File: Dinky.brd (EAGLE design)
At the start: 46.4 x 16.5 mm, 15 parts, among them IC1 SAMD21

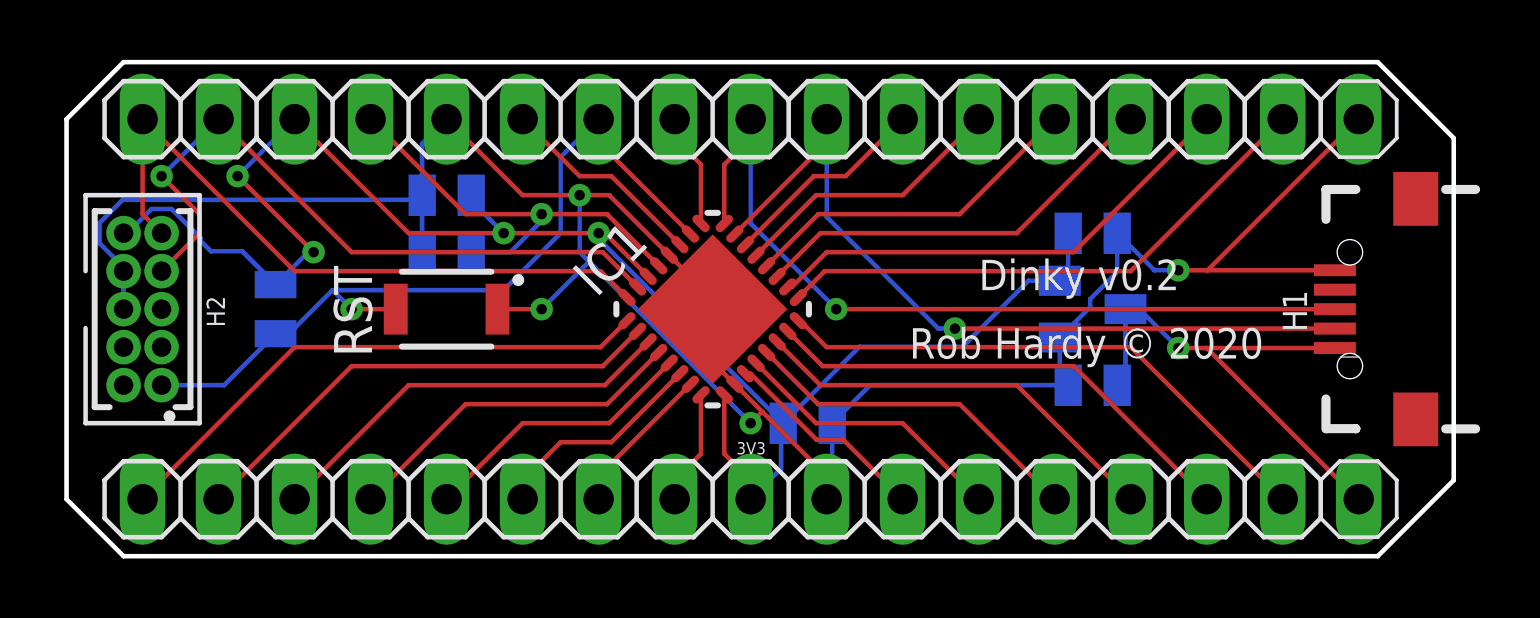
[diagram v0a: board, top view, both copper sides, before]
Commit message: Pin names
Mainly pin names and a bit of shuffling about
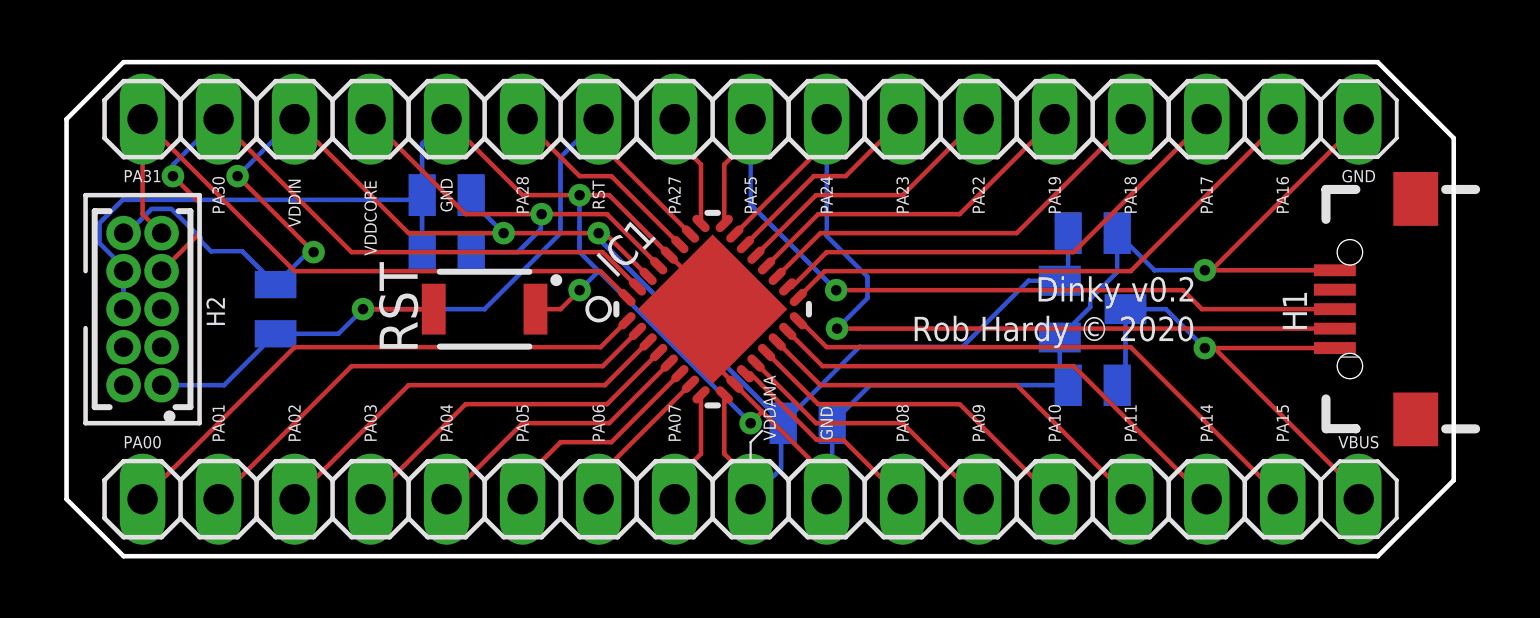
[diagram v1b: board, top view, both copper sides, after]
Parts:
- moved RST 1.27 mm to (14.0, 7.62)
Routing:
- net S$10: track 26.9 -> 29.7 mm
- net S$23: track 83.8 -> 82.8 mm
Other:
- board text added: "GND"
- board text added: "PA00"
- board text added: "PA01"
- board text added: "PA02"
- board text added: "PA03"
- board text added: "PA04"
- board text added: "PA05"
- board text added: "PA06"
- board text added: "PA07"
- board text added: "PA08"
- board text added: "PA09"
- board text added: "PA10"
- board text added: "PA11"
- board text added: "PA14"
- board text added: "PA15"
- board text added: "PA16"
- board text added: "PA17"
- board text added: "PA18"
- board text added: "PA19"
- board text added: "PA22"
- board text added: "PA23"
- board text added: "PA24"
- board text added: "PA25"
- board text added: "PA27"
- board text added: "PA28"
- board text added: "PA30"
- board text added: "PA31"
- board text added: "RST"
- board text added: "VBUS"
- board text added: "VDDANA"
- board text added: "VDDCORE"
- board text added: "VDDIN"
- board text removed: "3V3"

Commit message: Changed Button, Added LED, Added optional OSC32
Changed reset button to one more available and cheap (C&K KSR221G LFS).
Added ChipLED 0805 Red 1.8v LED to PA15 and a 100ohm resistor.
Also added pads for optional 32k osc/crystal on underside on pads PA00, PA01. Currently configured for Microcrystal CM7V-T1A and 2 12pf caps, but pads should take many combinations of crystal and caps,
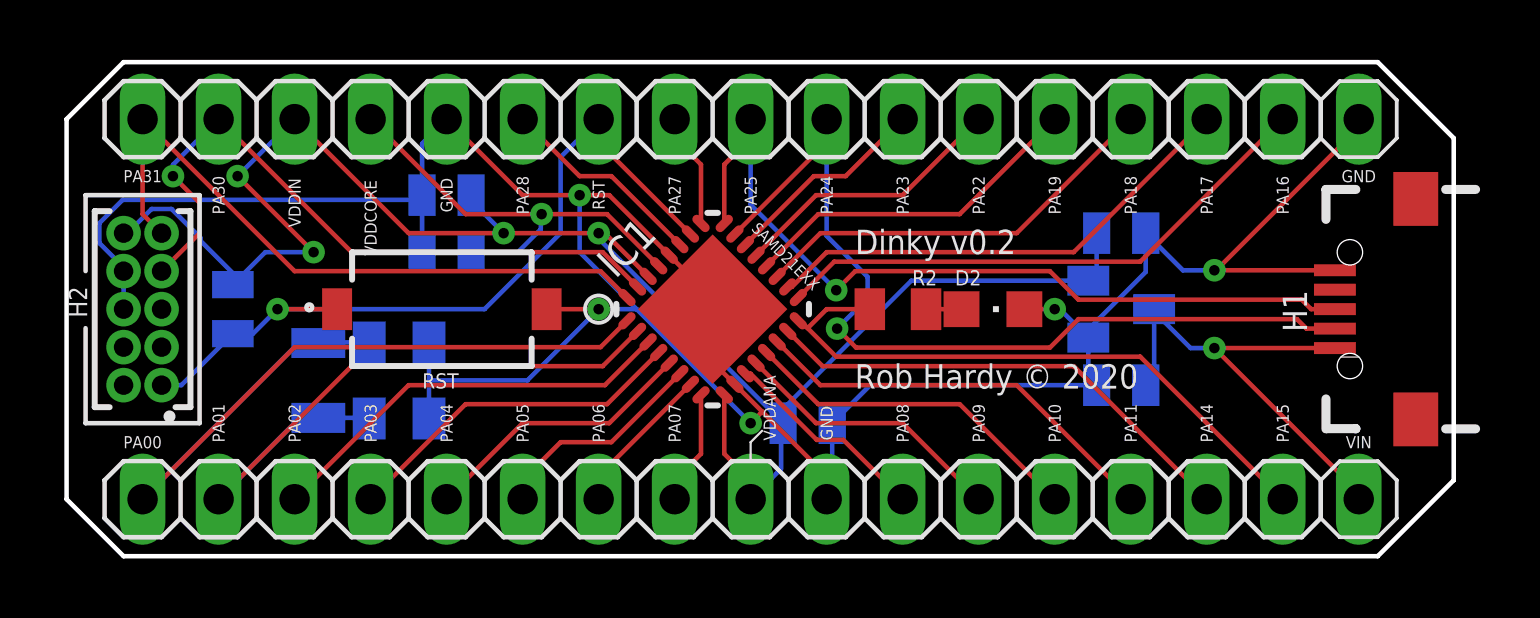
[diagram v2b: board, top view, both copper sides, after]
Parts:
- added C6, C7: (no value), adafruit:C0805K
- added D2: (no value), adafruit:CHIPLED_0805
- added R2: (no value), smd-ipc:R0805
- added Y1: (no value), CM7V-T1A-32.768kHz-12.5pF-20PP:CM7V-T1A
- RST: device B3U1000P:B3U-1000P -> KSR221G_LFS:KSR
- moved RST 1.43 mm to (12.5, 7.62)
- moved R1 1.43 mm to (5.56, 7.62)
- moved C1 0.95 mm to (35.2, 10.2)
- moved C2 0.95 mm to (35.2, 5.08)
- moved REG 0.95 mm to (35.2, 7.62)
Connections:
- removed net S$31: E$2.2, IC1.2
- removed net S$32: E$2.1, IC1.1
- new net S$24: C6.2, E$2.1, IC1.1, Y1.2
- new net S$34: C7.2, E$2.2, IC1.2, Y1.1
- new net S$5: D2.A, R2.2
- net S$17: now also R2.1
- net S$23: now also C6.1, C7.1, D2.C, RST.2; no longer RST.1
- net S$7: now also RST.1; no longer RST.2
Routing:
- net S$24: track 0.00 -> 28.4 mm
- net S$34: track 0.00 -> 22.5 mm
- net S$32: track 18.7 -> 0.00 mm
- net S$31: track 16.3 -> 0.00 mm
- net S$23: track 82.8 -> 94.7 mm, vias 4 -> 5
- net S$17: track 18.7 -> 21.0 mm
- net S$3: track 58.9 -> 60.4 mm
- net S$33: track 17.6 -> 16.3 mm
- net S$5: track 0.00 -> 1.18 mm
- net S$10: track 29.7 -> 30.5 mm
- net S$9: track 27.7 -> 28.2 mm
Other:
- board text added: "SAMD21EXX"
- board text added: "VIN"
- board text removed: "VBUS"

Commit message: Pin numbering. Larger silk text.
Changed pin numbering to minimal. Enlarged font for silkscreen printing. Moved small component names under placement as unrequired outside of placement and saves space for larger pin names and other text.
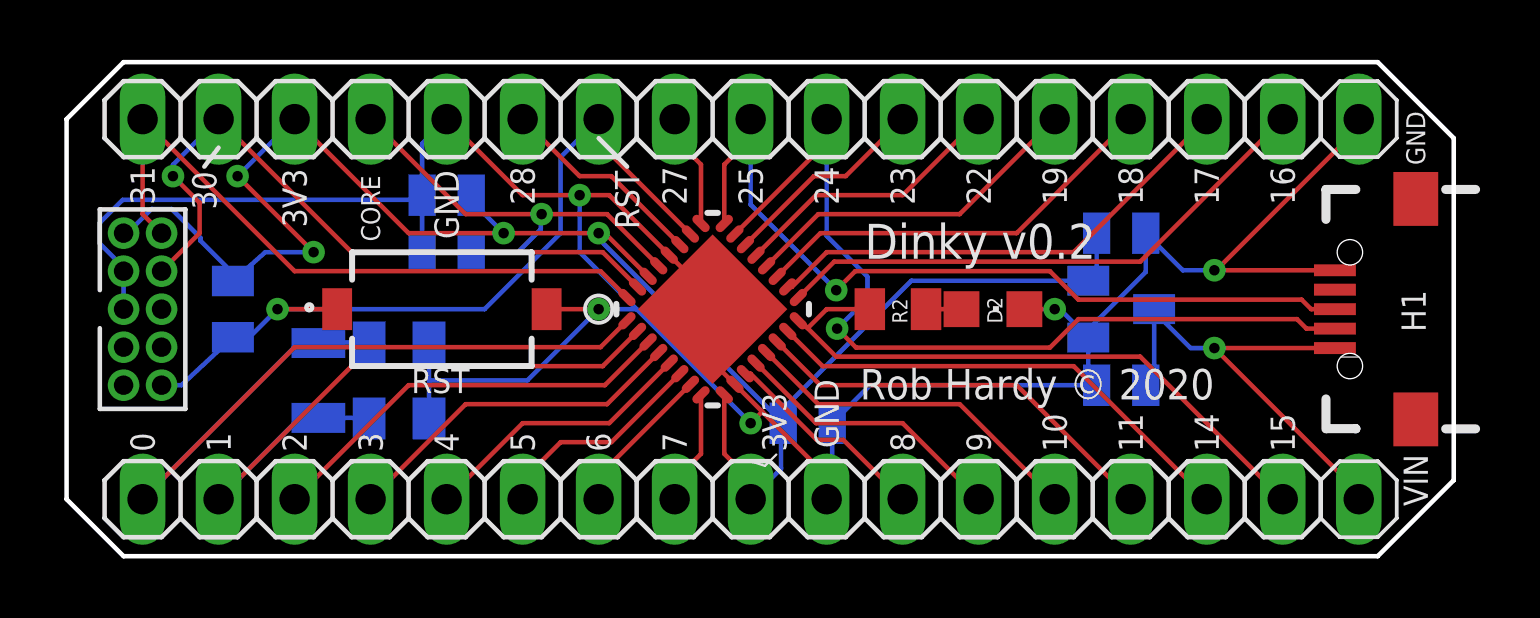
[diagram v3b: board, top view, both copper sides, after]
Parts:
- removed H2: (no value), o163734v244 Eagle_WR-PHD (rev19a):62201021821
- R1: device GRM2165C1H471JA01J:CAPC2012X70N -> smd-ipc:R0805
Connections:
- net S$1: no longer H2.9
- net S$2: no longer H2.7
- net S$23: no longer H2.6, H2.8
- net S$3: no longer H2.10
- net S$7: no longer H2.1
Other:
- board text added: "0"
- board text added: "1"
- board text added: "10"
- board text added: "11"
- board text added: "14"
- board text added: "15"
- board text added: "16"
- board text added: "17"
- board text added: "18"
- board text added: "19"
- board text added: "2"
- board text added: "22"
- board text added: "23"
- board text added: "24"
- board text added: "25"
- board text added: "27"
- board text added: "28"
- board text added: "3"
- board text added: "30"
- board text added: "31"
- board text added: "3V3"
- board text added: "4"
- board text added: "5"
- board text added: "6"
- board text added: "7"
- board text added: "8"
- board text added: "9"
- board text added: "CORE"
- board text removed: "PA00"
- board text removed: "PA01"
- board text removed: "PA02"
- board text removed: "PA03"
- board text removed: "PA04"
- board text removed: "PA05"
- board text removed: "PA06"
- board text removed: "PA07"
- board text removed: "PA08"
- board text removed: "PA09"
- board text removed: "PA10"
- board text removed: "PA11"
- board text removed: "PA14"
- board text removed: "PA15"
- board text removed: "PA16"
- board text removed: "PA17"
- board text removed: "PA18"
- board text removed: "PA19"
- board text removed: "PA22"
- board text removed: "PA23"
- board text removed: "PA24"
- board text removed: "PA25"
- board text removed: "PA27"
- board text removed: "PA28"
- board text removed: "PA30"
- board text removed: "PA31"
- board text removed: "SAMD21EXX"
- board text removed: "VDDANA"
- board text removed: "VDDCORE"
- board text removed: "VDDIN"

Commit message: Changed usb connector
Changed the usb connector for a stronger one. Some silk changes.

Added CAM data zip file.
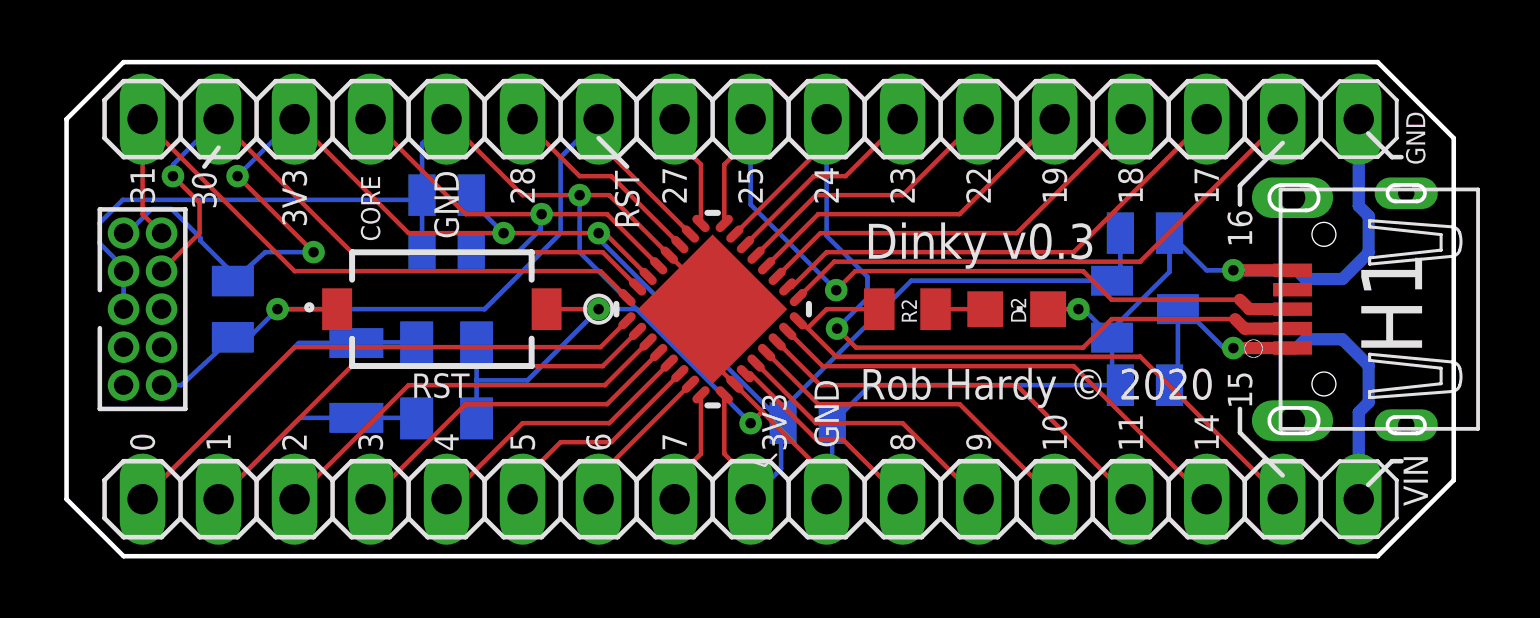
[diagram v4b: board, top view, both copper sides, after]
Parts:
- H1: device MicroUSB:USB-MICRO-SMD -> Wurth_Elektronik_Electromechanic_Input-Output_Connectors_rev16a:629105150521
- moved C6 1.59 mm to (12.7, 6.51)
- moved C7 1.59 mm to (12.7, 3.97)
- moved Y1 1.27 mm to (9.68, 5.24)
- moved C1 0.79 mm to (36.0, 10.2)
- moved C2 0.79 mm to (36.0, 5.08)
- moved REG 0.79 mm to (36.0, 7.62)
- moved D2 0.79 mm to (31.8, 7.62)
- moved H1 0.32 mm to (44.8, 7.62), turned to 90 degrees
- moved R2 0.32 mm to (28.1, 7.62)
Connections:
- net S$10: now also H1.2; no longer H1.D-1
- net S$23: now also H1.5; no longer H1.GND1
- net S$33: now also H1.1; no longer H1.VBUS1
- net S$9: now also H1.3; no longer H1.D+1
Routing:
- net S$34: track 22.5 -> 24.1 mm
- net S$24: track 28.4 -> 30.0 mm
- net S$10: track 30.5 -> 29.1 mm
- net S$9: track 28.2 -> 26.8 mm
- net S$3: track 60.2 -> 60.9 mm
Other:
- board text added: "Dinky v0.3"
- board text removed: "Dinky v0.2"
